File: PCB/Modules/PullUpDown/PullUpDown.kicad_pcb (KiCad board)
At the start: 2 copper layers, 29 x 59 mm, 60 parts, among them J1 In, J2 In, Q1 Q_PMOS_GSD, Q10 Q_NMOS_GSD, Q11 Q_PMOS_GSD, Q12 Q_NMOS_GSD, Q13 Q_PMOS_GSD, Q14 Q_NMOS_GSD, Q15 Q_PMOS_GSD, Q16 Q_NMOS_GSD, Q2 Q_NMOS_GSD, Q3 Q_PMOS_GSD, Q4 Q_NMOS_GSD, Q5 Q_PMOS_GSD, Q6 Q_NMOS_GSD, Q7 Q_PMOS_GSD, Q8 Q_NMOS_GSD, Q9 Q_PMOS_GSD, U1 SP720ABTG

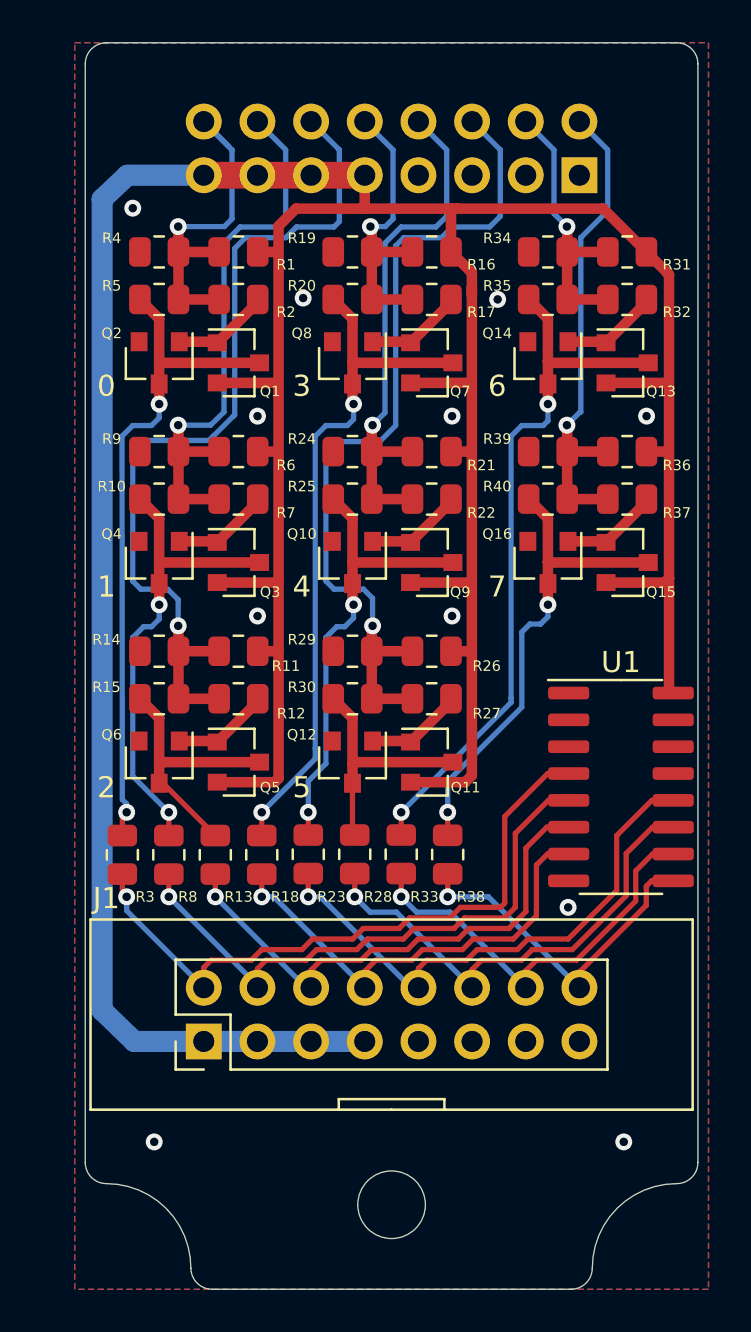
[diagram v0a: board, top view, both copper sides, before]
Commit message: Convert all KiCad to 6.0, clean up libraries, remove files that shouldn't be committed.
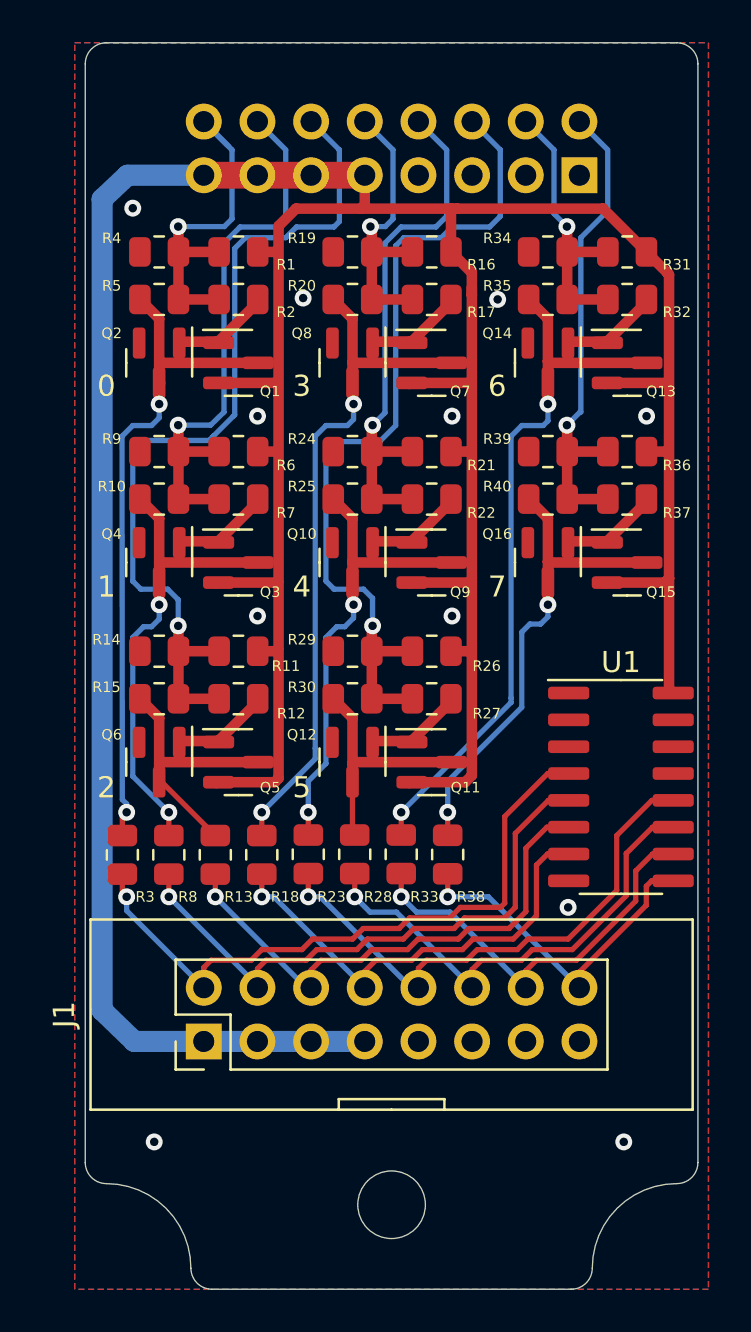
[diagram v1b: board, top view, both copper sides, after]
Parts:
- J1, J2: footprint Custom:PinHeader_2x08_P2.54mm_Vertical-Centered -> KTANE:PinHeader_2x08_P2.54mm_Vertical-Centered
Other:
- net class Default removed
- net class v Power removed

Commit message: First pass of PCB rework.
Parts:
- removed the R10 at (24.0, 42.1)
- removed the R15 at (24.0, 51.5)
- removed the R20 at (33.1, 32.6)
- removed the R25 at (33.1, 42.1)
- removed the R30 at (33.1, 51.5)
- removed R35, R40: 0, Resistor_SMD:R_0805_2012Metric
- removed the R5 at (24.0, 32.6)
- removed REF**: MountingHole_3.2mm_M3, MountingHole:MountingHole_3.2mm_M3
- added JP1: Bypass, Jumper:SolderJumper-2_P1.3mm_Open_RoundedPad1.0x1.5mm, F.Cu at (133.2, 42.9)
- added JP10: V2, Jumper:SolderJumper-3_P1.3mm_Open_RoundedPad1.0x1.5mm, F.Cu at (112.9, 43.6)
- added JP11: V1, Jumper:SolderJumper-3_P1.3mm_Open_RoundedPad1.0x1.5mm, F.Cu at (105.2, 39.8)
- added JP12: V2, Jumper:SolderJumper-3_P1.3mm_Open_RoundedPad1.0x1.5mm, F.Cu at (105.2, 43.6)
- added JP13: V1, Jumper:SolderJumper-3_P1.3mm_Open_RoundedPad1.0x1.5mm, F.Cu at (105.2, 49.5)
- added JP14: V2, Jumper:SolderJumper-3_P1.3mm_Open_RoundedPad1.0x1.5mm, F.Cu at (105.2, 53.3)
- added JP15: V1, Jumper:SolderJumper-3_P1.3mm_Open_RoundedPad1.0x1.5mm, F.Cu at (105.2, 30.1)
- added JP16: V2, Jumper:SolderJumper-3_P1.3mm_Open_RoundedPad1.0x1.5mm, F.Cu at (105.2, 34.0)
- added JP17: V1, Jumper:SolderJumper-3_P1.3mm_Open_RoundedPad1.0x1.5mm, F.Cu at (120.5, 30.1)
- added JP18: V2, Jumper:SolderJumper-3_P1.3mm_Open_RoundedPad1.0x1.5mm, F.Cu at (120.5, 34.0)
- added JP19: V1, Jumper:SolderJumper-3_P1.3mm_Open_RoundedPad1.0x1.5mm, F.Cu at (112.9, 49.5)
- added JP2: Bypass, Jumper:SolderJumper-2_P1.3mm_Open_RoundedPad1.0x1.5mm, F.Cu at (128.2, 39.8)
- added JP20: V2, Jumper:SolderJumper-3_P1.3mm_Open_RoundedPad1.0x1.5mm, F.Cu at (112.9, 53.3)
- added JP21: V1, Jumper:SolderJumper-3_P1.3mm_Open_RoundedPad1.0x1.5mm, F.Cu at (128.2, 30.1)
- added JP22: V2, Jumper:SolderJumper-3_P1.3mm_Open_RoundedPad1.0x1.5mm, F.Cu at (128.2, 34.0)
- added JP23: V1, Jumper:SolderJumper-3_P1.3mm_Open_RoundedPad1.0x1.5mm, F.Cu at (112.9, 30.1)
- added JP24: V2, Jumper:SolderJumper-3_P1.3mm_Open_RoundedPad1.0x1.5mm, F.Cu at (112.9, 34.0)
- added JP3: Bypass, Jumper:SolderJumper-2_P1.3mm_Open_RoundedPad1.0x1.5mm, F.Cu at (120.5, 45.6)
- added JP4: Bypass, Jumper:SolderJumper-2_P1.3mm_Open_RoundedPad1.0x1.5mm, F.Cu at (128.2, 45.6)
- added JP5: Bypass, Jumper:SolderJumper-2_P1.3mm_Open_RoundedPad1.0x1.5mm, F.Cu at (120.5, 51.4)
- added JP6: Bypass, Jumper:SolderJumper-2_P1.3mm_Open_RoundedPad1.0x1.5mm, F.Cu at (120.5, 57.3)
- added JP7: Bypass, Jumper:SolderJumper-2_P1.3mm_Open_RoundedPad1.0x1.5mm, F.Cu at (128.2, 51.4)
- added JP8: Bypass, Jumper:SolderJumper-2_P1.3mm_Open_RoundedPad1.0x1.5mm, F.Cu at (128.2, 57.3)
- added JP9: V1, Jumper:SolderJumper-3_P1.3mm_Open_RoundedPad1.0x1.5mm, F.Cu at (112.9, 39.8)
- moved Q10 43.7 mm to (76.8, 44.5)
- moved Q11 43.7 mm to (80.6, 54.0)
- moved Q12 43.7 mm to (76.8, 54.0)
- moved Q13 43.7 mm to (89.8, 35.1)
- moved Q14 43.7 mm to (86.1, 35.1)
- moved Q15 43.7 mm to (89.8, 44.5)
- moved Q16 43.7 mm to (86.1, 44.5)
- moved Q7 43.7 mm to (80.6, 35.1)
- moved Q8 43.7 mm to (76.8, 35.1)
- moved Q9 43.7 mm to (80.6, 44.5)
- moved R12 43.7 mm to (70.3, 58.4)
- moved R13 43.7 mm to (80.6, 29.8)
- moved R14 43.7 mm to (76.8, 29.8)
- moved R15 43.7 mm to (80.6, 32.1)
- moved R17 43.7 mm to (80.6, 39.3)
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- renumbered J2 to J1, J1 to J2, R14 to R10, R12 to R11, R13 to R12, R16 to R13, R19 to R14, R17 to R15, R18 to R16, R21 to R17, R24 to R18, R22 to R19, R4 to R2, R23 to R20, R26 to R21, R29 to R22, R27 to R23, R28 to R24, R31 to R25, R34 to R26, R32 to R27, R33 to R28, R36 to R29, R2 to R3, R39 to R30, R37 to R31, R38 to R32, R3 to R4, R6 to R5, R9 to R6, R11 to R9
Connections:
- J1 pad 11: +5V -> I2C-CLK
- J1 pad 13: +5V -> +3.3V
- J1 pad 3: GND -> SPI-CIPO
- J1 pad 5: GND -> SPI-COPI
- J1 pad 7: GND -> SPI-CLK
- J1 pad 9: +5V -> I2C-DAT
- J2 pad 1: +5V -> LR1
- J2 pad 11: GND -> LR6
- J2 pad 13: GND -> LR7
- J2 pad 15: GND -> LR8
- J2 pad 3: +5V -> LR2
- J2 pad 5: +5V -> LR3
- J2 pad 7: +5V -> LR4
- J2 pad 9: GND -> LR5
- Q1 pad 2: +5V -> VCC
- Q11 pad 2: +5V -> VCC
- Q13 pad 2: +5V -> VCC
- Q15 pad 2: +5V -> VCC
- Q3 pad 2: +5V -> VCC
- Q5 pad 2: +5V -> VCC
- Q7 pad 2: +5V -> VCC
- Q9 pad 2: +5V -> VCC
- R1 pad 2: +5V -> +3.3V
- R13 pad 2: +5V -> +3.3V
- R17 pad 2: +5V -> +3.3V
- R21 pad 2: +5V -> +3.3V
- R25 pad 2: +5V -> +3.3V
- R29 pad 2: +5V -> +3.3V
- R5 pad 2: +5V -> +3.3V
- R9 pad 2: +5V -> +3.3V
- U1 pad 10: O6 -> I6
- U1 pad 11: O5 -> I5
- U1 pad 12: O4 -> I4
- U1 pad 16: +5V -> +3.3V
- U1 pad 4: O0 -> I0
- U1 pad 5: O1 -> I1
- U1 pad 6: O2 -> I2
- U1 pad 7: O3 -> I3
- U1 pad 9: O7 -> I7
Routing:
- net +5V: track 188.7 -> 0.00 mm
- net I2: track 41.5 -> 0.00 mm, vias 1 -> 0
- net I5: track 40.2 -> 0.00 mm, vias 1 -> 0
- net Net-(JP7-B): track 34.0 -> 0.00 mm, vias 2 -> 0
- net Net-(JP4-B): track 32.9 -> 0.00 mm, vias 2 -> 0
- net Net-(JP1-B): track 32.0 -> 0.00 mm, vias 2 -> 0
- net O0: track 31.4 -> 0.00 mm, vias 1 -> 0
- net O1: track 28.1 -> 0.00 mm, vias 1 -> 0
- net I1: track 26.4 -> 0.00 mm, vias 1 -> 0
- net O4: track 25.9 -> 0.00 mm, vias 1 -> 0
- net O2: track 25.0 -> 0.00 mm, vias 1 -> 0
- net I4: track 24.7 -> 0.00 mm, vias 1 -> 0
- net Net-(JP8-B): track 23.3 -> 0.00 mm, vias 2 -> 0
- net I7: track 23.1 -> 0.00 mm, vias 1 -> 0
- net O5: track 22.8 -> 0.00 mm, vias 1 -> 0
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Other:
- board text added: "Rev B01"
- board text removed: "0"
- board text removed: "1"
- board text removed: "2"
- board text removed: "3"
- board text removed: "4"
- board text removed: "5"
- board text removed: "7"
- board text removed: "Direct"
- board text removed: "FET Inrush"
- board text removed: "High FET"
- board text removed: "Limit"
- board text removed: "Low FET"
- board text removed: "Port Config Layout"
- board text removed: "Pull Down"
- board text removed: "Pull Up"
- board text removed: "Q1"
- board text removed: "Q2"
- board text removed: "R1"
- board text removed: "R2"
- board text removed: "R3"
- board text removed: "R4"
- board text removed: "R5"
- board text removed: "Rev A04"

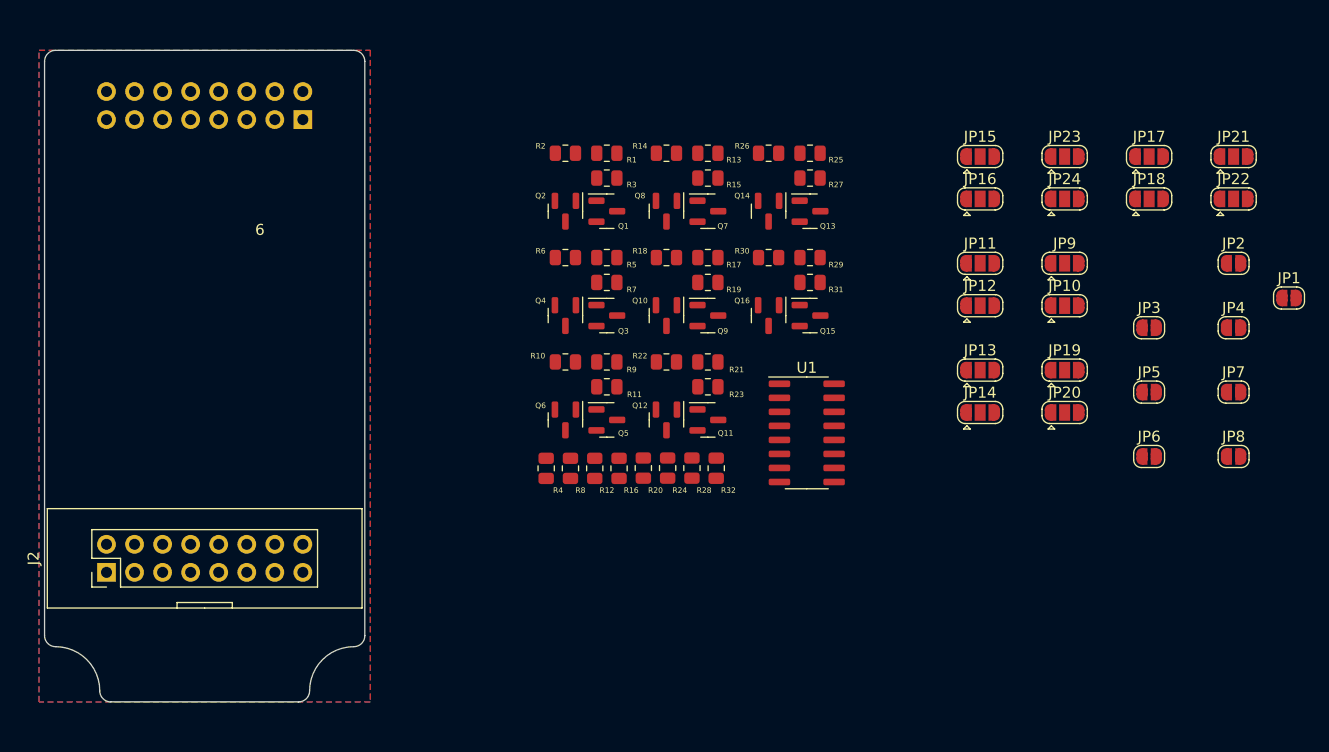
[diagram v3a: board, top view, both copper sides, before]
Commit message: Update pull up/down module, with multivoltage ESD protection.
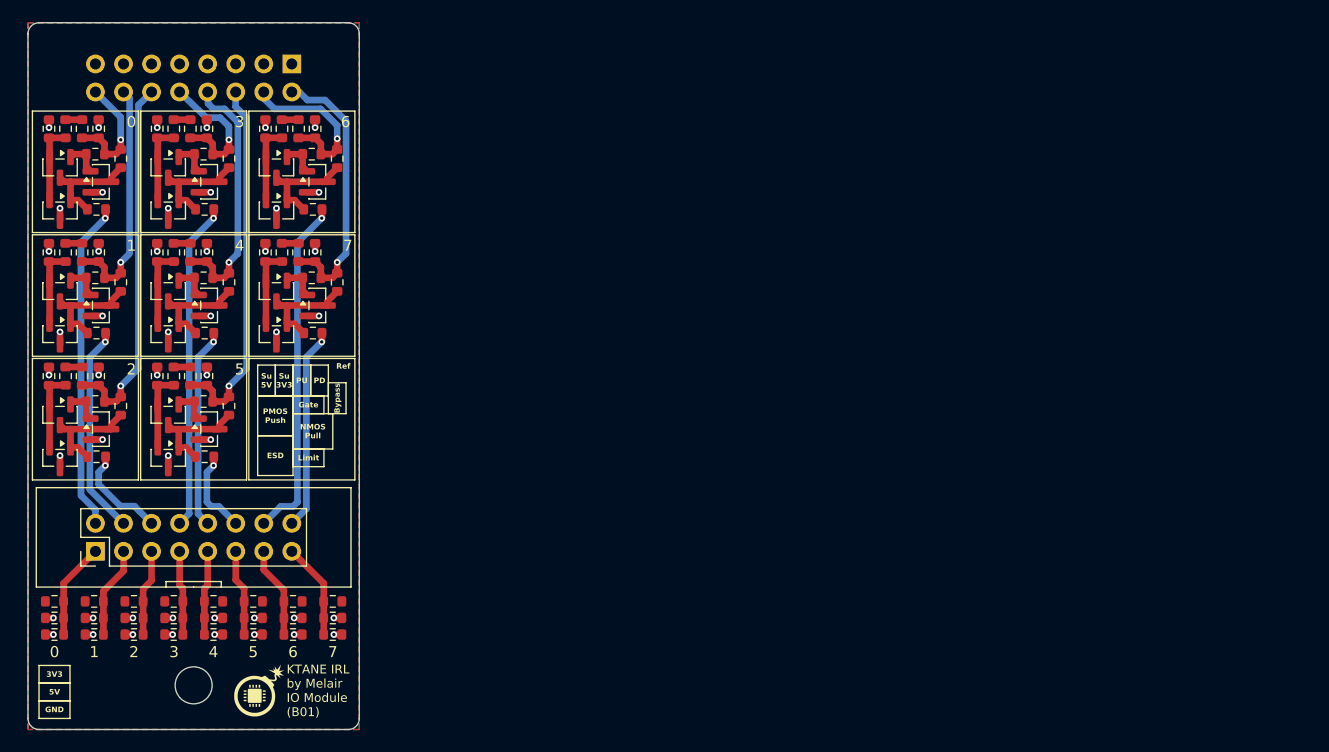
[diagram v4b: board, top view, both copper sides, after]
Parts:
- removed JP1, JP2, JP3, JP4, JP5, JP6, JP7, JP8: Bypass, Jumper:SolderJumper-2_P1.3mm_Open_RoundedPad1.0x1.5mm
- removed JP10, JP12, JP14, JP16, JP18, JP20, JP22, JP24: V2, Jumper:SolderJumper-3_P1.3mm_Open_RoundedPad1.0x1.5mm
- removed JP11, JP13, JP15, JP17, JP19, JP21, JP23, JP9: V1, Jumper:SolderJumper-3_P1.3mm_Open_RoundedPad1.0x1.5mm
- removed U1: SP720ABTG, Package_SO:SOIC-16_3.9x9.9mm_P1.27mm
- added D1: D1213A-01SO-7, Package_TO_SOT_SMD:SOT-23, F.Cu at (21.9, 35.0)
- added D2: D1213A-01SO-7, Package_TO_SOT_SMD:SOT-23, F.Cu at (21.9, 46.2)
- added D3: D1213A-01SO-7, Package_TO_SOT_SMD:SOT-23, F.Cu at (21.9, 57.4)
- added D4: D1213A-01SO-7, Package_TO_SOT_SMD:SOT-23, F.Cu at (31.7, 35.0)
- added D5: D1213A-01SO-7, Package_TO_SOT_SMD:SOT-23, F.Cu at (31.7, 46.2)
- added D6: D1213A-01SO-7, Package_TO_SOT_SMD:SOT-23, F.Cu at (31.7, 57.4)
- added D7: D1213A-01SO-7, Package_TO_SOT_SMD:SOT-23, F.Cu at (41.5, 35.0)
- added D8: D1213A-01SO-7, Package_TO_SOT_SMD:SOT-23, F.Cu at (41.5, 46.2)
- added G***: LOGO, KTANE:KTANEIRL-0505, F.Cu at (40.0, 78.5)
- added R1: 0, Resistor_SMD:R_0603_1608Metric, F.Cu at (20.9, 27.6)
- added R14: 0, Resistor_SMD:R_0603_1608Metric, F.Cu at (27.4, 41.5)
- added R15: 0, Resistor_SMD:R_0603_1608Metric, F.Cu at (20.9, 50.0)
- added R16: 0, Resistor_SMD:R_0603_1608Metric, F.Cu at (22.4, 50.0)
- added R2: 0, Resistor_SMD:R_0603_1608Metric, F.Cu at (22.4, 27.6)
- added R21: 0, Resistor_SMD:R_0603_1608Metric, F.Cu at (27.4, 52.7)
- added R22: 0, Resistor_SMD:R_0603_1608Metric, F.Cu at (30.7, 27.6)
- added R23: 0, Resistor_SMD:R_0603_1608Metric, F.Cu at (32.2, 27.6)
- added R28: 0, Resistor_SMD:R_0603_1608Metric, F.Cu at (37.2, 30.3)
- added R29: 0, Resistor_SMD:R_0603_1608Metric, F.Cu at (30.7, 38.8)
- added R30: 0, Resistor_SMD:R_0603_1608Metric, F.Cu at (32.2, 38.8)
- added R35: 0, Resistor_SMD:R_0603_1608Metric, F.Cu at (37.2, 41.5)
- added R36: 0, Resistor_SMD:R_0603_1608Metric, F.Cu at (30.7, 50.0)
- added R37: 0, Resistor_SMD:R_0603_1608Metric, F.Cu at (32.2, 50.0)
- added R42: 0, Resistor_SMD:R_0603_1608Metric, F.Cu at (37.2, 52.7)
- added R43: 0, Resistor_SMD:R_0603_1608Metric, F.Cu at (40.5, 27.6)
- added R44: 0, Resistor_SMD:R_0603_1608Metric, F.Cu at (42.0, 27.6)
- added R49: 0, Resistor_SMD:R_0603_1608Metric, F.Cu at (47.0, 30.3)
- added R50: 0, Resistor_SMD:R_0603_1608Metric, F.Cu at (40.5, 38.8)
- added R51: 0, Resistor_SMD:R_0603_1608Metric, F.Cu at (42.0, 38.8)
- added R56: 0, Resistor_SMD:R_0603_1608Metric, F.Cu at (47.0, 41.5)
- added R57: 0, Resistor_SMD:R_0603_1608Metric, F.Cu at (21.4, 71.9)
- added R58: 0, Resistor_SMD:R_0603_1608Metric, F.Cu at (21.4, 70.4)
- added R60: 0, Resistor_SMD:R_0603_1608Metric, F.Cu at (21.4, 73.4)
- added R61: 0, Resistor_SMD:R_0603_1608Metric, F.Cu at (25.0, 71.9)
- added R62: 0, Resistor_SMD:R_0603_1608Metric, F.Cu at (25.0, 70.4)
- added R64: 0, Resistor_SMD:R_0603_1608Metric, F.Cu at (25.0, 73.4)
- added R65: 0, Resistor_SMD:R_0603_1608Metric, F.Cu at (28.6, 71.9)
- added R66: 0, Resistor_SMD:R_0603_1608Metric, F.Cu at (28.6, 70.4)
- added R68: 0, Resistor_SMD:R_0603_1608Metric, F.Cu at (28.6, 73.4)
- added R69: 0, Resistor_SMD:R_0603_1608Metric, F.Cu at (32.2, 71.9)
- added R7: 0, Resistor_SMD:R_0603_1608Metric, F.Cu at (27.4, 30.3)
- added R70: 0, Resistor_SMD:R_0603_1608Metric, F.Cu at (32.2, 70.4)
- added R72: 0, Resistor_SMD:R_0603_1608Metric, F.Cu at (32.2, 73.4)
- added R73: 0, Resistor_SMD:R_0603_1608Metric, F.Cu at (35.8, 71.9)
- added R74: 0, Resistor_SMD:R_0603_1608Metric, F.Cu at (35.8, 70.4)
- added R76: 0, Resistor_SMD:R_0603_1608Metric, F.Cu at (35.8, 73.4)
- added R77: 0, Resistor_SMD:R_0603_1608Metric, F.Cu at (39.4, 71.9)
- added R78: 0, Resistor_SMD:R_0603_1608Metric, F.Cu at (39.4, 70.4)
- added R8: 0, Resistor_SMD:R_0603_1608Metric, F.Cu at (20.9, 38.8)
- added R80: 0, Resistor_SMD:R_0603_1608Metric, F.Cu at (39.4, 73.4)
- added R81: 0, Resistor_SMD:R_0603_1608Metric, F.Cu at (43.0, 71.9)
- added R82: 0, Resistor_SMD:R_0603_1608Metric, F.Cu at (43.0, 70.4)
- added R84: 0, Resistor_SMD:R_0603_1608Metric, F.Cu at (43.0, 73.4)
- added R85: 0, Resistor_SMD:R_0603_1608Metric, F.Cu at (46.6, 71.9)
- added R86: 0, Resistor_SMD:R_0603_1608Metric, F.Cu at (46.6, 70.4)
- added R88: 0, Resistor_SMD:R_0603_1608Metric, F.Cu at (46.6, 73.4)
- added R9: 0, Resistor_SMD:R_0603_1608Metric, F.Cu at (22.4, 38.8)
- J1: value In -> Out; moved to F.Cu
- J2: footprint KTANE:PinHeader_2x08_P2.54mm_Vertical-Centered -> KTANE:KTANE Submodule Connector V2 - Short
- R10: renamed from R5; footprint Resistor_SMD:R_0805_2012Metric -> Resistor_SMD:R_0603_1608Metric
- R11: renamed from R7; footprint Resistor_SMD:R_0805_2012Metric -> Resistor_SMD:R_0603_1608Metric
- R12: renamed from R8; footprint Resistor_SMD:R_0805_2012Metric -> Resistor_SMD:R_0603_1608Metric
- R13: renamed from R6; footprint Resistor_SMD:R_0805_2012Metric -> Resistor_SMD:R_0603_1608Metric
- R17: renamed from R9; footprint Resistor_SMD:R_0805_2012Metric -> Resistor_SMD:R_0603_1608Metric
- R18: renamed from R11; footprint Resistor_SMD:R_0805_2012Metric -> Resistor_SMD:R_0603_1608Metric
- R19: renamed from R12; footprint Resistor_SMD:R_0805_2012Metric -> Resistor_SMD:R_0603_1608Metric
- R20: renamed from R10; footprint Resistor_SMD:R_0805_2012Metric -> Resistor_SMD:R_0603_1608Metric
- R24: renamed from R13; footprint Resistor_SMD:R_0805_2012Metric -> Resistor_SMD:R_0603_1608Metric
- R25: renamed from R15; footprint Resistor_SMD:R_0805_2012Metric -> Resistor_SMD:R_0603_1608Metric
- R26: renamed from R16; footprint Resistor_SMD:R_0805_2012Metric -> Resistor_SMD:R_0603_1608Metric
- R27: renamed from R14; footprint Resistor_SMD:R_0805_2012Metric -> Resistor_SMD:R_0603_1608Metric
- R3: renamed from R1; footprint Resistor_SMD:R_0805_2012Metric -> Resistor_SMD:R_0603_1608Metric
- R31: renamed from R17; footprint Resistor_SMD:R_0805_2012Metric -> Resistor_SMD:R_0603_1608Metric
- R32: renamed from R19; footprint Resistor_SMD:R_0805_2012Metric -> Resistor_SMD:R_0603_1608Metric
- R33: renamed from R20; footprint Resistor_SMD:R_0805_2012Metric -> Resistor_SMD:R_0603_1608Metric
- R34: renamed from R18; footprint Resistor_SMD:R_0805_2012Metric -> Resistor_SMD:R_0603_1608Metric
- R38: renamed from R21; footprint Resistor_SMD:R_0805_2012Metric -> Resistor_SMD:R_0603_1608Metric
- R39: renamed from R23; footprint Resistor_SMD:R_0805_2012Metric -> Resistor_SMD:R_0603_1608Metric
- R4: renamed from R3; footprint Resistor_SMD:R_0805_2012Metric -> Resistor_SMD:R_0603_1608Metric
- R40: renamed from R24; footprint Resistor_SMD:R_0805_2012Metric -> Resistor_SMD:R_0603_1608Metric
- R41: renamed from R22; footprint Resistor_SMD:R_0805_2012Metric -> Resistor_SMD:R_0603_1608Metric
- R45: renamed from R25; footprint Resistor_SMD:R_0805_2012Metric -> Resistor_SMD:R_0603_1608Metric
- R46: renamed from R27; footprint Resistor_SMD:R_0805_2012Metric -> Resistor_SMD:R_0603_1608Metric
- R47: renamed from R28; footprint Resistor_SMD:R_0805_2012Metric -> Resistor_SMD:R_0603_1608Metric
- R48: renamed from R26; footprint Resistor_SMD:R_0805_2012Metric -> Resistor_SMD:R_0603_1608Metric
- R5: renamed from R4; footprint Resistor_SMD:R_0805_2012Metric -> Resistor_SMD:R_0603_1608Metric
- R52: renamed from R29; footprint Resistor_SMD:R_0805_2012Metric -> Resistor_SMD:R_0603_1608Metric
- R53: renamed from R31; footprint Resistor_SMD:R_0805_2012Metric -> Resistor_SMD:R_0603_1608Metric
- R54: renamed from R32; footprint Resistor_SMD:R_0805_2012Metric -> Resistor_SMD:R_0603_1608Metric
- R55: renamed from R30; footprint Resistor_SMD:R_0805_2012Metric -> Resistor_SMD:R_0603_1608Metric
- R6: renamed from R2; footprint Resistor_SMD:R_0805_2012Metric -> Resistor_SMD:R_0603_1608Metric
- moved Q1 49.7 mm to (21.9, 31.1), turned to -90 degrees
- moved Q3 49.6 mm to (21.9, 42.3), turned to -90 degrees
- moved Q5 49.5 mm to (21.9, 53.5), turned to -90 degrees
- moved Q7 49.0 mm to (31.7, 31.1), turned to -90 degrees
- moved Q9 48.9 mm to (31.7, 42.3), turned to -90 degrees
- moved Q11 48.9 mm to (31.7, 53.5), turned to -90 degrees
- moved Q13 48.5 mm to (41.5, 31.1), turned to -90 degrees
- moved Q15 48.4 mm to (41.5, 42.3), turned to -90 degrees
- moved R3 47.6 mm to (23.9, 27.6), turned to 90 degrees
- moved R17 47.5 mm to (23.9, 50.0), turned to 90 degrees
- moved R10 47.5 mm to (23.9, 38.8), turned to 90 degrees
- moved R5 47.0 mm to (25.2, 34.9), turned to 180 degrees
- moved R24 46.9 mm to (33.7, 27.6), turned to 90 degrees
- moved R38 46.9 mm to (33.7, 50.0), turned to 90 degrees
- moved R31 46.9 mm to (33.7, 38.8), turned to 90 degrees
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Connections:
- J1 pad 1: GND -> LR1
- J1 pad 10: I3 -> O4
- J1 pad 11: I2C-CLK -> LR6
- J1 pad 12: I2 -> O5
- J1 pad 13: +3.3V -> LR7
- J1 pad 14: I1 -> O6
- J1 pad 15: +5V -> LR8
- J1 pad 16: I0 -> O7
- J1 pad 2: I7 -> O0
- J1 pad 3: SPI-CIPO -> LR2
- J1 pad 4: I6 -> O1
- J1 pad 5: SPI-COPI -> LR3
- J1 pad 6: I5 -> O2
- J1 pad 7: SPI-CLK -> LR4
- J1 pad 8: I4 -> O3
- J1 pad 9: I2C-DAT -> LR5
- J2 pad 1: LR1 -> SPI-CIPO
- J2 pad 10: O4 -> I3
- J2 pad 11: LR6 -> GND
- J2 pad 12: O5 -> I2
- J2 pad 13: LR7 -> +5V
- J2 pad 14: O6 -> I1
- J2 pad 15: LR8 -> +3.3V
- J2 pad 16: O7 -> I0
- J2 pad 2: O0 -> I7
- J2 pad 3: LR2 -> SPI-CLK
- J2 pad 4: O1 -> I6
- J2 pad 5: LR3 -> SPI-COPI
- J2 pad 6: O2 -> I5
- J2 pad 7: LR4 -> I2C-DAT
- J2 pad 8: O3 -> I4
- J2 pad 9: LR5 -> I2C-CLK
- Q1 pad 2: VCC -> Net-(Q1-S)
- Q11 pad 2: VCC -> Net-(Q11-S)
- Q13 pad 2: VCC -> Net-(Q13-S)
- Q15 pad 2: VCC -> Net-(Q15-S)
- Q3 pad 2: VCC -> Net-(Q3-S)
- Q5 pad 2: VCC -> Net-(Q5-S)
- Q7 pad 2: VCC -> Net-(Q7-S)
- Q9 pad 2: VCC -> Net-(Q9-S)
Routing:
- net I2: track 0.00 -> 33.6 mm, vias 0 -> 1
- net I5: track 0.00 -> 33.5 mm, vias 0 -> 1
- net O6: track 0.00 -> 31.3 mm, vias 0 -> 1
- net O0: track 0.00 -> 29.9 mm, vias 0 -> 1
- net O3: track 0.00 -> 29.7 mm, vias 0 -> 1
- net GND: track 0.00 -> 29.4 mm, vias 0 -> 32
- net I7: track 0.00 -> 24.9 mm, vias 0 -> 1
- net I4: track 0.00 -> 23.3 mm, vias 0 -> 1
- net I1: track 0.00 -> 21.7 mm, vias 0 -> 1
- net O1: track 0.00 -> 19.1 mm, vias 0 -> 1
- net O7: track 0.00 -> 18.4 mm, vias 0 -> 1
- net O4: track 0.00 -> 18.2 mm, vias 0 -> 1
- net I6: track 0.00 -> 15.3 mm, vias 0 -> 1
- net I3: track 0.00 -> 12.7 mm, vias 0 -> 1
- net +3.3V: track 0.00 -> 12.0 mm
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- added copper zone on F.Cu, net +3.3V
- added copper zone on B.Cu, net +5V
- added copper zone on In1.Cu, net GND
- added copper zone on In2.Cu, net GND
- removed copper zone on B.Cu, net GND
- removed copper zone on F.Cu, net GND
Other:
- board size 29 x 59 mm -> 30 x 64 mm
- copper layers 2 -> 4
- board text added: "0"
- board text added: "1"
- board text added: "2"
- board text added: "3"
- board text added: "3V3"
- board text added: "4"
- board text added: "5"
- board text added: "5V"
- board text added: "7"
- board text added: "Bypass"
- board text added: "ESD"
- board text added: "GND"
- board text added: "Gate"
- board text added: "KTANE IRL by Melair IO Module (B01)"
- board text added: "Limit"
- board text added: "NMOS Pull"
- board text added: "PD"
- board text added: "PMOS Push"
- board text added: "PU"
- board text added: "Ref"
- board text added: "Su 3V3"
- board text added: "Su 5V"
- board text removed: "Keep Talking and Nobody Explodes IO Module"
- board text removed: "Module Config"
- board text removed: "Rev B01"
